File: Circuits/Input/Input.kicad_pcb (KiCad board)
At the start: 2 copper layers, 28.9 x 68.9 mm, 7 parts, among them P1 WRITER-VCC, U1 TWE-Lite_SMD

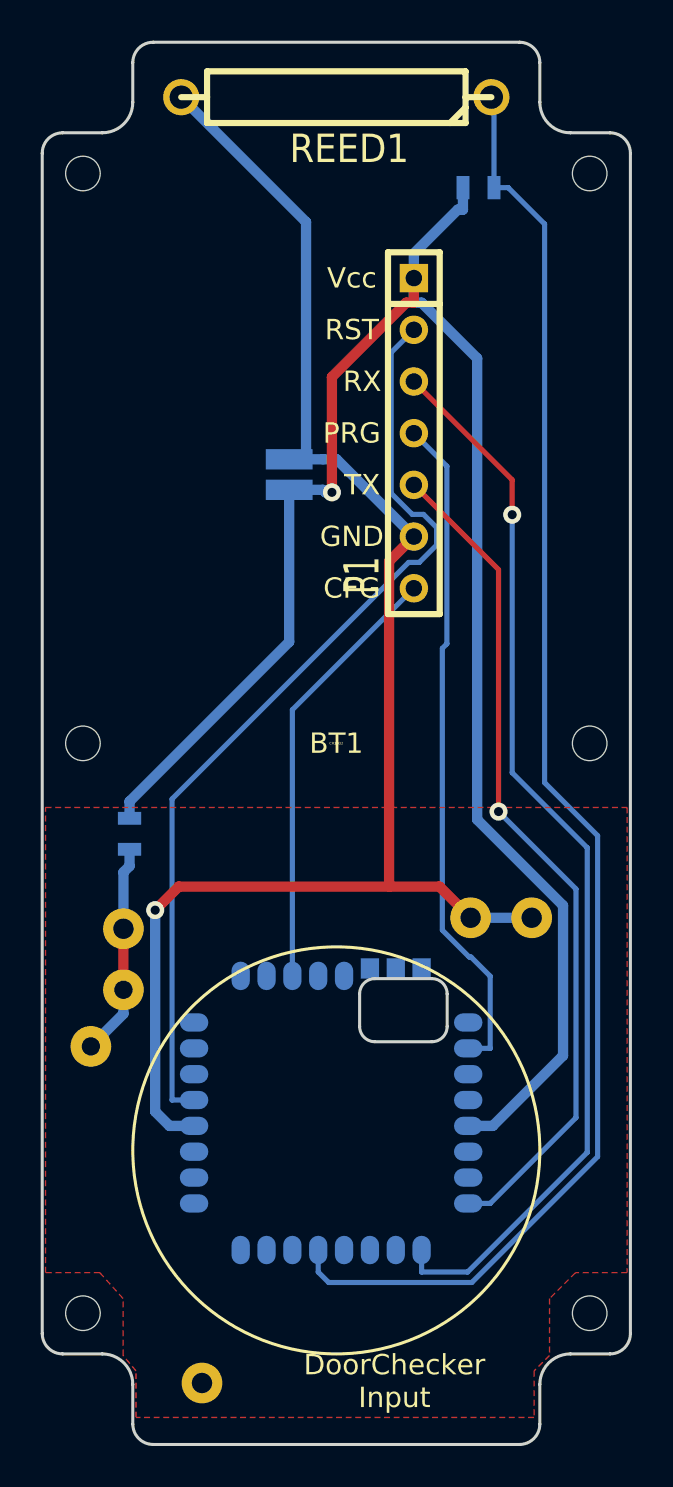
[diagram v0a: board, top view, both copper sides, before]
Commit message: Replaced a EDLC to an array of MLCC.
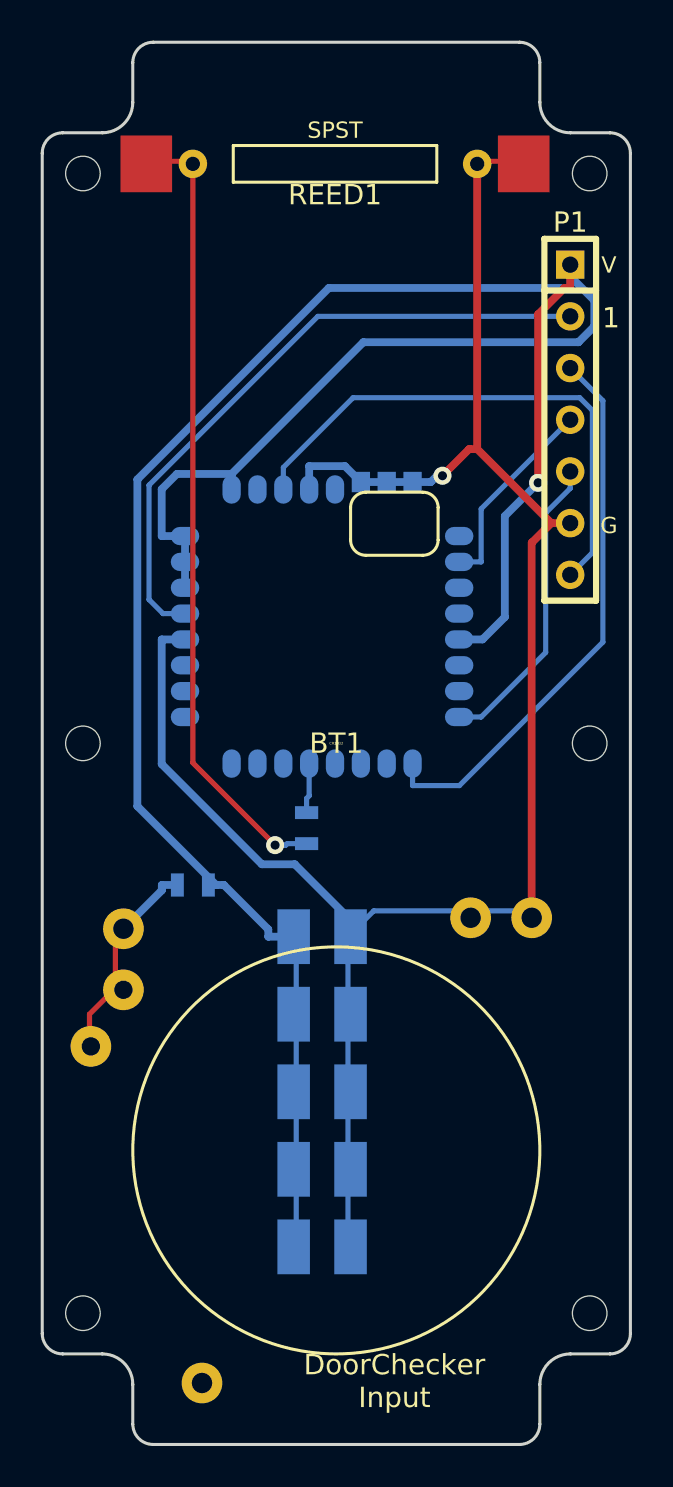
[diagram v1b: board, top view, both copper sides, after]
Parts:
- added C2: 100u, c_1210, B.Cu at (27.9, 62.2)
- added C3: 100u, c_1210, B.Cu at (27.9, 66.0)
- added C4: 100u, c_1210, B.Cu at (27.9, 69.8)
- added C5: 100u, c_1210, B.Cu at (27.9, 73.7)
- C1: value 0.22 -> 100u; footprint DCK-3R3E224-E -> c_1210
- P1: footprint 2211R-07G-LP -> WRITE-7P
- REED1: footprint R6 -> REEDSW
- U1: value TWE-Lite_SMD -> TWE_LITE_SMD; footprint TWE-001L-SMD -> TWE-001L-SMD-noNTH
- moved R1 32.6 mm to (27.2, 53.1), turned to 270 degrees
- moved U1 23.9 mm to (27.9, 43.2)
- moved C1 23.7 mm to (27.9, 58.4), turned to 180 degrees
- moved P1 7.71 mm to (40.1, 33.0)
- moved R2 4.00 mm to (21.6, 55.9), turned to 0 degrees
- moved REED1 3.28 mm to (28.6, 20.4)
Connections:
- P1 pad 1: VCC -> /RST
- P1 pad 2: /RST -> /RXD
- P1 pad 3: /RXD -> /PRG
- P1 pad 4: /PRG -> /TXD
- P1 pad 5: /TXD -> GND
- P1 pad 6: GND -> /CFG
- R1 pad 1: /DOOR -> /DI1
- R1 pad 2: VCC -> /DOOR
- REED1 pad 1: /DOOR -> GND
- REED1 pad 2: GND -> /DOOR
- U1 pad 13: /DOOR -> /DI1
- U1 pad 22: (no net) -> VCC
- U1 pad 23: (no net) -> VCC
- U1 pad 24: (no net) -> VCC
- U1 pad 25: (no net) -> VCC
- U1 pad 28: (no net) -> GND
- U1 pad 30: (no net) -> GND
- U1 pad 31: (no net) -> GND
- U1 pad 32: (no net) -> GND
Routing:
- net VCC: track 87.1 -> 125.1 mm
- net /DOOR: track 72.2 -> 39.7 mm, vias 0 -> 1
- net /TXD: track 41.4 -> 15.0 mm, vias 1 -> 0
- net /RXD: track 53.1 -> 27.5 mm, vias 1 -> 0
- net GND: track 77.4 -> 100.7 mm
- net /PRG: track 33.1 -> 9.88 mm
- net /RST: track 46.3 -> 31.8 mm
- net /CFG: track 21.5 -> 26.5 mm
- net /DI1: track 0.00 -> 2.46 mm
- net /DC3V: track 10.5 -> 11.0 mm
- removed copper zone on F.Cu, net (none)
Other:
- net class power: trace_width 0.508 -> 0.384
- board text removed: "CFG"
- board text removed: "GND"
- board text removed: "PRG"
- board text removed: "RST"
- board text removed: "RX"
- board text removed: "TX"
- board text removed: "Vcc"

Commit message: Added a voltage monitor.
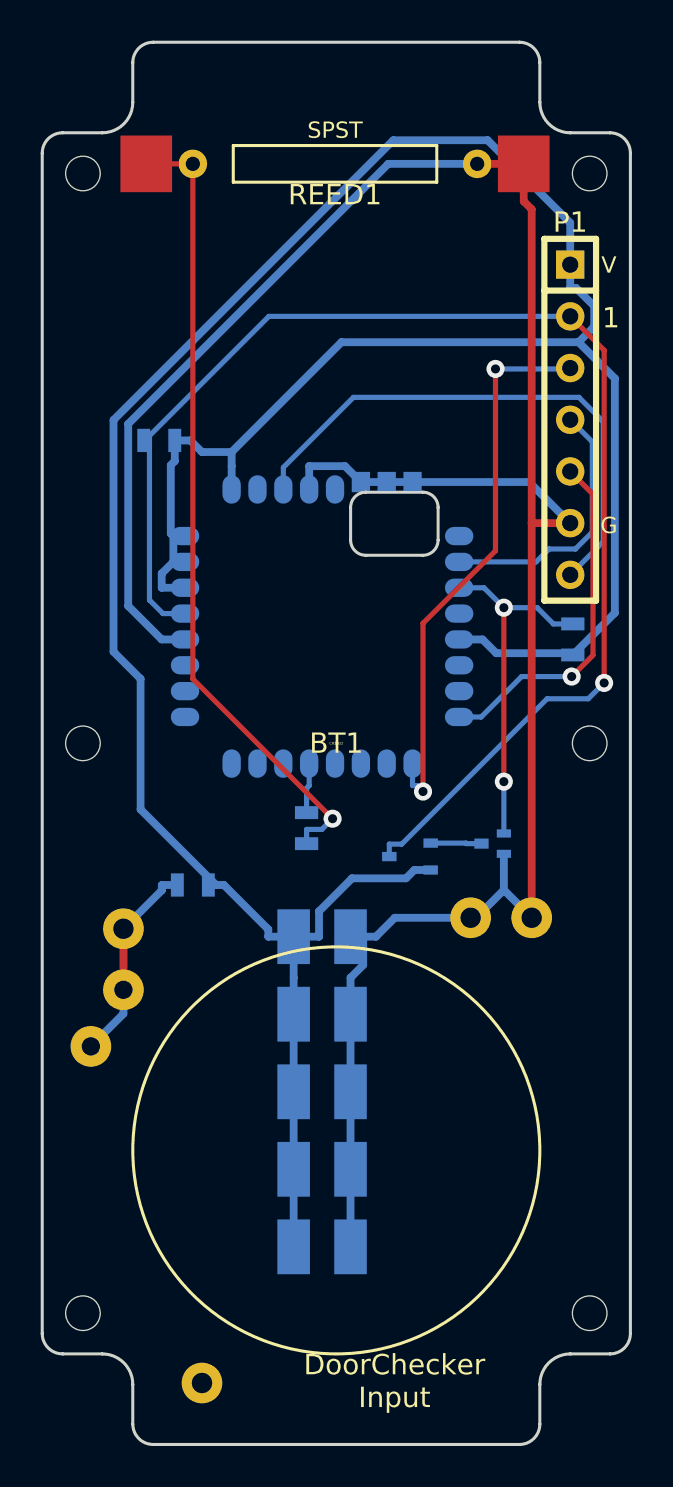
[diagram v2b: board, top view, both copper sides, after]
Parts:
- added Q1: MOS_N, EMT3, B.Cu at (36.3, 53.8)
- added R3: 10M, SM0603_Resistor, B.Cu at (40.3, 43.8)
- added R4: 10M, SM0603_Resistor, B.Cu at (19.9, 34.0)
- added U2: TCM809RVNB, sc70, B.Cu at (32.3, 54.5)
- R1, R2: footprint SM0603 -> SM0603_Resistor
- U1: footprint TWE-001L-SMD-noNTH -> TWE-001L-NC7
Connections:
- U1 pad 3: (no net) -> /DO1
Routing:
- net /RST: track 31.8 -> 66.6 mm, vias 0 -> 1
- net VCC: track 125.1 -> 148.0 mm, vias 1 -> 0
- net GND: track 100.7 -> 119.1 mm, vias 1 -> 0
- net /DO1: track 0.00 -> 17.4 mm, vias 0 -> 2
- net /PRG: track 9.88 -> 13.1 mm
- net /QGND: track 0.00 -> 2.51 mm
- net /TXD: track 15.0 -> 17.3 mm, vias 0 -> 1
- net /DC3V: track 11.0 -> 10.1 mm
- net /RXD: track 27.5 -> 27.6 mm, vias 0 -> 2

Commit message: Fixed: Switch to configuration mode by M2.
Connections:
- U1 pad 26: (no net) -> /CFG
- U1 pad 27: /CFG -> (no net)
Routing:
- net /CFG: track 26.9 -> 28.2 mm
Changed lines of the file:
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@@
     (thickness 1)
     (drawings 3)
-    (tracks 161)
+    (tracks 162)
     (zones 0)
     (modules 15)
@@
     (pad 26 smd oval (at 3.175 6.735 180) (size 0.9 1.4)
       (layers B.Cu B.Paste B.Mask)
+      (net 1 /CFG)
     )
     (pad 27 smd oval (at 1.905 6.735 180) (size 0.9 1.4)
       (layers B.Cu B.Paste B.Mask)
-      (net 1 /CFG)
     )
     (pad 28 smd oval (at 0.635 6.735 180) (size 0.9 1.4)
@@
     (arrow2b (pts (xy 48.96438 83.358617) (xy 48.377544 82.23233)))
   )
-  (segment (start 26.035 36.445) (end 26.035 35.3637) (width 0.254) (layer B.Cu) (net 1))
+  (segment (start 24.765 36.445) (end 24.765 35.306) (width 0.254) (layer B.Cu) (net 1) (status 400000))
+  (segment (start 29.4786 31.9201) (end 40.56 31.9201) (width 0.254) (layer B.Cu) (net 1))
+  (segment (start 40.56 31.9201) (end 41.7506 33.1107) (width 0.254) (layer B.Cu) (net 1))
+  (segment (start 41.7506 33.1107) (end 41.7506 39.0214) (width 0.254) (layer B.Cu) (net 1))
   (segment (start 41.7506 39.0214) (end 40.132 40.64) (width 0.254) (layer B.Cu) (net 1))
-  (segment (start 41.7506 33.1107) (end 41.7506 39.0214) (width 0.254) (layer B.Cu) (net 1))
-  (segment (start 40.56 31.9201) (end 41.7506 33.1107) (width 0.254) (layer B.Cu) (net 1))
-  (segment (start 29.4786 31.9201) (end 40.56 31.9201) (width 0.254) (layer B.Cu) (net 1))
-  (segment (start 26.035 35.3637) (end 29.4786 31.9201) (width 0.254) (layer B.Cu) (net 1))
+  (segment (start 28.1509 31.9201) (end 29.4786 31.9201) (width 0.254) (layer B.Cu) (net 1))
+  (segment (start 24.765 35.306) (end 28.1509 31.9201) (width 0.254) (layer B.Cu) (net 1))
   (segment (start 20.0642 56.1447) (end 18.1785 58.0304) (width 0.384) (layer B.Cu) (net 2))
   (segment (start 20.0642 55.88) (end 20.0642 56.1447) (width 0.384) (layer B.Cu) (net 2))

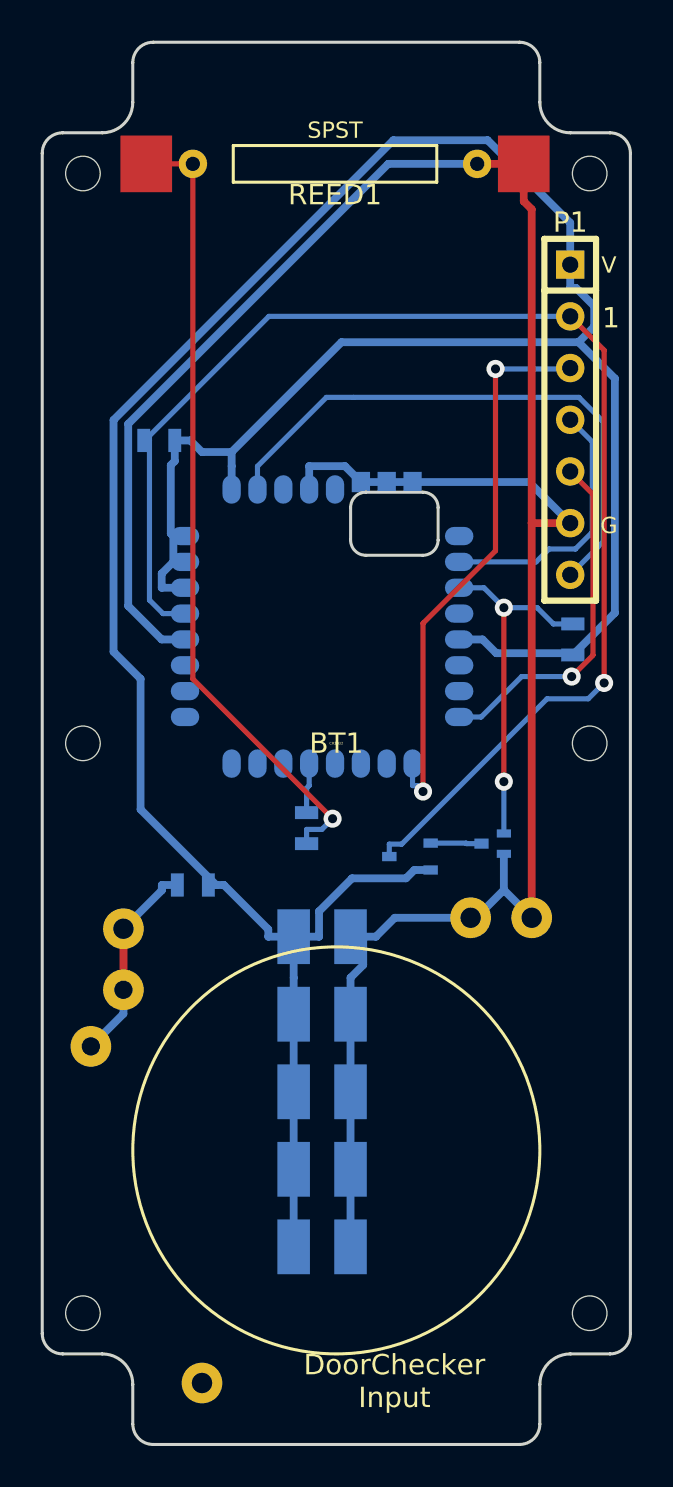
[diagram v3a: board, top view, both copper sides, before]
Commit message: Migrating to current version of KiCad.
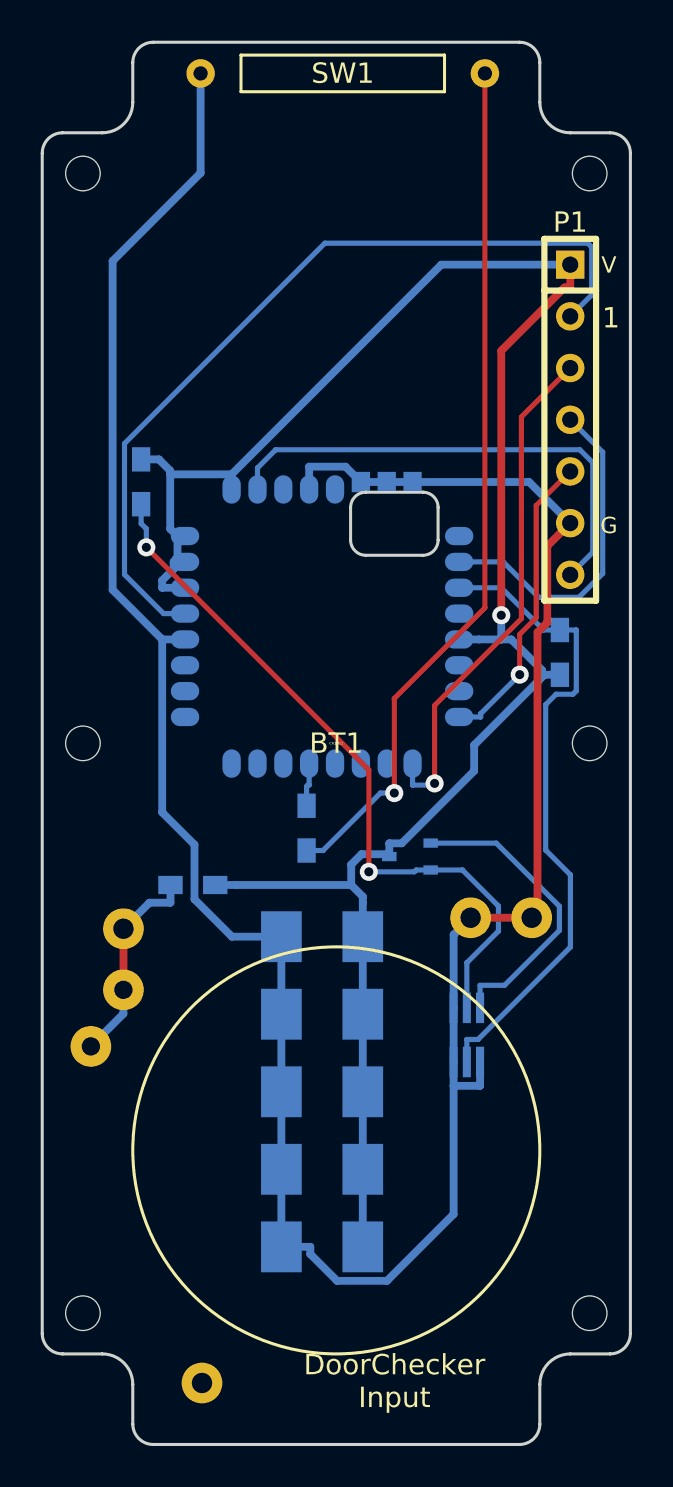
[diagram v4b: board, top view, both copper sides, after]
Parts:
- removed Q1: MOS_N, EMT3
- removed REED1: SPST, REEDSW
- added SW1: MKA-10110, favorites:MKA-10110, F.Cu at (29.0, 16.0)
- added U3: 2N7002DW, Housings_SOT-23_SOT-143_TSOT-6:SC-70-6_Handsoldering, B.Cu at (35.1, 63.2)
- BT1: footprint PBCS-75 -> favorites:PBCS-75
- C1, C2, C3, C4, C5: footprint c_1210 -> Capacitors_SMD:C_1210_HandSoldering
- P1: footprint WRITE-7P -> favorites:WRITE-7P
- R1, R3, R4: footprint SM0603_Resistor -> Resistors_SMD:R_0603_HandSoldering
- R2: value 75 -> 1k; footprint SM0603_Resistor -> Resistors_SMD:R_0603_HandSoldering
- U1: footprint TWE-001L-NC7 -> favorites:TWE-001L-NC7
- U2: footprint sc70 -> Transistors_SMD:sc70
- moved R4 2.22 mm to (19.1, 36.1), turned to 270 degrees
- moved R3 0.90 mm to (39.6, 44.5)
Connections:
- R1 pad 2: /DOOR -> Net-(R1-Pad2)
- R4 pad 2: /RST -> /RESET#
- U1 pad 1: (no net) -> Net-(U1-Pad1)
- U1 pad 10: (no net) -> Net-(U1-Pad10)
- U1 pad 11: (no net) -> Net-(U1-Pad11)
- U1 pad 12: (no net) -> Net-(U1-Pad12)
- U1 pad 14: (no net) -> Net-(U1-Pad14)
- U1 pad 15: (no net) -> Net-(U1-Pad15)
- U1 pad 16: (no net) -> Net-(U1-Pad16)
- U1 pad 17: (no net) -> Net-(U1-Pad17)
- U1 pad 18: (no net) -> Net-(U1-Pad18)
- U1 pad 19: (no net) -> Net-(U1-Pad19)
- U1 pad 27: (no net) -> Net-(U1-Pad27)
- U1 pad 29: (no net) -> Net-(U1-Pad29)
- U1 pad 4: (no net) -> Net-(U1-Pad4)
- U1 pad 6: (no net) -> Net-(U1-Pad6)
- U1 pad 7: (no net) -> Net-(U1-Pad7)
- U2 pad 2: /RST -> /RESET#
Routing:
- net VCC: track 148.0 -> 100.5 mm, vias 0 -> 1
- net Net-(R1-Pad2): track 0.00 -> 42.7 mm, vias 0 -> 1
- net /DOOR: track 39.5 -> 0.00 mm, vias 1 -> 0
- net /RESET#: track 0.00 -> 35.5 mm, vias 0 -> 2
- net /RST: track 66.6 -> 41.2 mm, vias 1 -> 0
- net /DO1: track 17.4 -> 31.9 mm, vias 2 -> 0
- net GND: track 119.1 -> 131.8 mm
- net /QGND: track 2.51 -> 14.9 mm
- net /CFG: track 28.2 -> 24.1 mm
- net /PRG: track 13.1 -> 16.5 mm
- net /TXD: track 17.3 -> 14.9 mm
- net /RXD: track 27.6 -> 25.3 mm, vias 2 -> 1
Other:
- net class Default: clearance 0.254 -> 0.229
- net class power: clearance 0.254 -> 0.229
- rule trace_clearance: 0.254 -> 0.229

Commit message: Simplified power supply block.
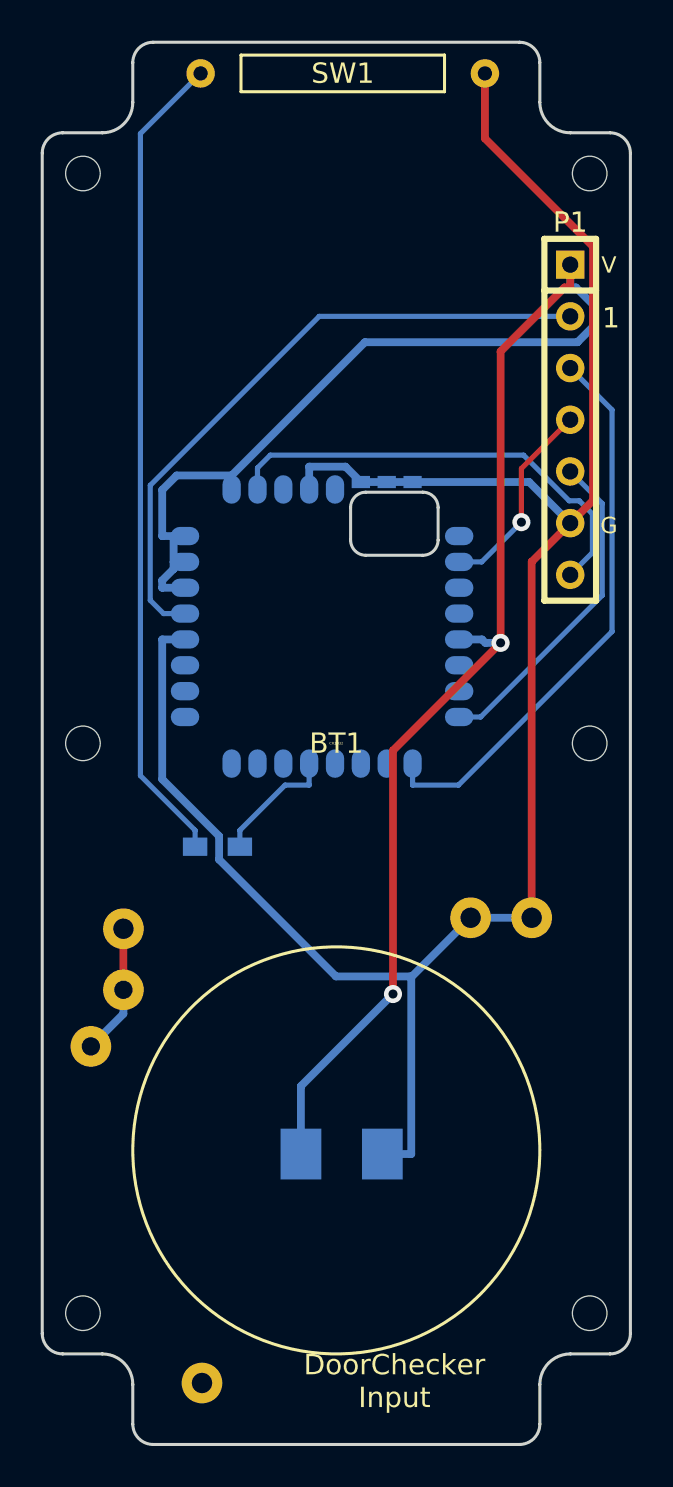
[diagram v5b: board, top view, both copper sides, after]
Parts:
- removed C2, C3, C4, C5: 100u, Capacitors_SMD:C_1210_HandSoldering
- removed R2: 1k, Resistors_SMD:R_0603_HandSoldering
- removed R3, R4: 10M, Resistors_SMD:R_0603_HandSoldering
- removed U2: TCM809RVNB, Transistors_SMD:sc70
- removed U3: 2N7002DW, Housings_SOT-23_SOT-143_TSOT-6:SC-70-6_Handsoldering
- moved C1 10.7 mm to (28.9, 69.1), turned to 0 degrees
- moved R1 4.47 mm to (22.8, 54.0), turned to 180 degrees
- turned SW1 to 180 degrees
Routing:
- net /RESET#: track 35.5 -> 0.00 mm, vias 2 -> 0
- net /DO1: track 31.9 -> 0.00 mm
- net GND: track 131.8 -> 102.2 mm
- net /QGND: track 14.9 -> 0.00 mm
- net VCC: track 100.5 -> 88.1 mm, vias 1 -> 2
- net /RST: track 41.2 -> 31.7 mm
- net /PRG: track 16.5 -> 9.89 mm, vias 0 -> 1
- net /DI1: track 2.16 -> 6.19 mm
- net /DC3V: track 10.2 -> 6.44 mm
- net /RXD: track 25.3 -> 27.8 mm, vias 1 -> 0
- net Net-(R1-Pad2): track 42.7 -> 40.3 mm, vias 1 -> 0
- net /CFG: track 24.1 -> 22.4 mm
- net /TXD: track 14.9 -> 16.2 mm, vias 1 -> 0
